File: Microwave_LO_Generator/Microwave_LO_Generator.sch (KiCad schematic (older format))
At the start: 0 parts

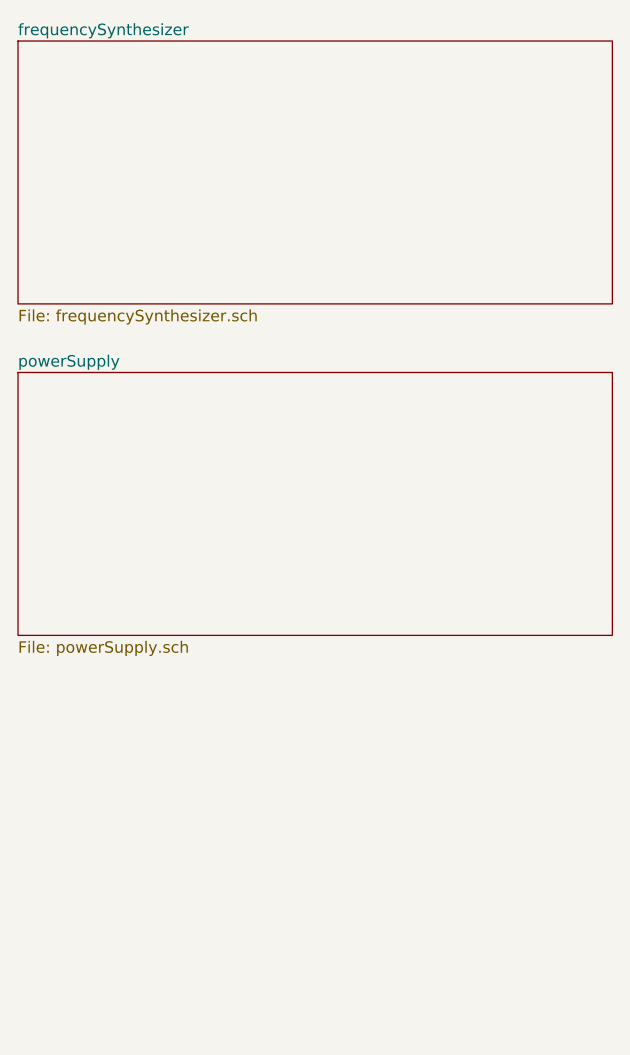
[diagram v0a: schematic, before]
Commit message: add vco
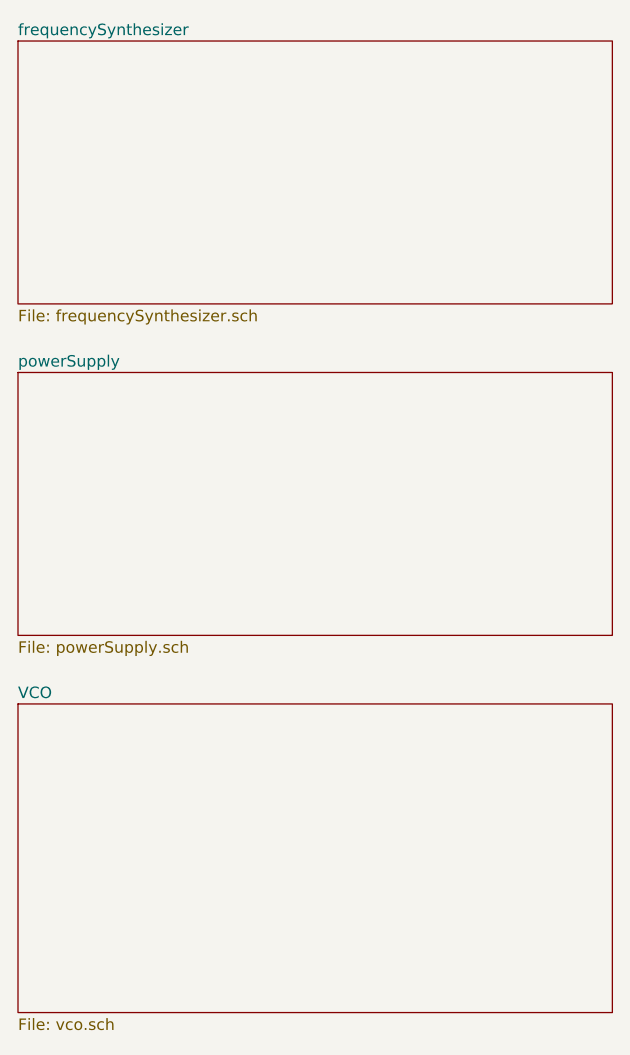
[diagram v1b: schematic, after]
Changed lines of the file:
@@
 $Descr A4 11693 8268
 encoding utf-8
-Sheet 1 3
+Sheet 1 4
 Title ""
 Date ""
@@
 F1 "powerSupply.sch" 50
 $EndSheet
+$Sheet
+S 900  3800 2600 1350
+U 5FC49510
+F0 "VCO" 50
+F1 "vco.sch" 50
+$EndSheet
 $EndSCHEMATC
